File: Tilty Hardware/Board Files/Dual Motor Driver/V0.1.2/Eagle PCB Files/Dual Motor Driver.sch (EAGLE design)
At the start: 42 parts, among them J1 AVR_SPI_PRG_62X3_LOCK, Q1 16MHz, U1 ATMEGA328P, U2 L298_BRIDGE_DRIVER, U3 LM2931

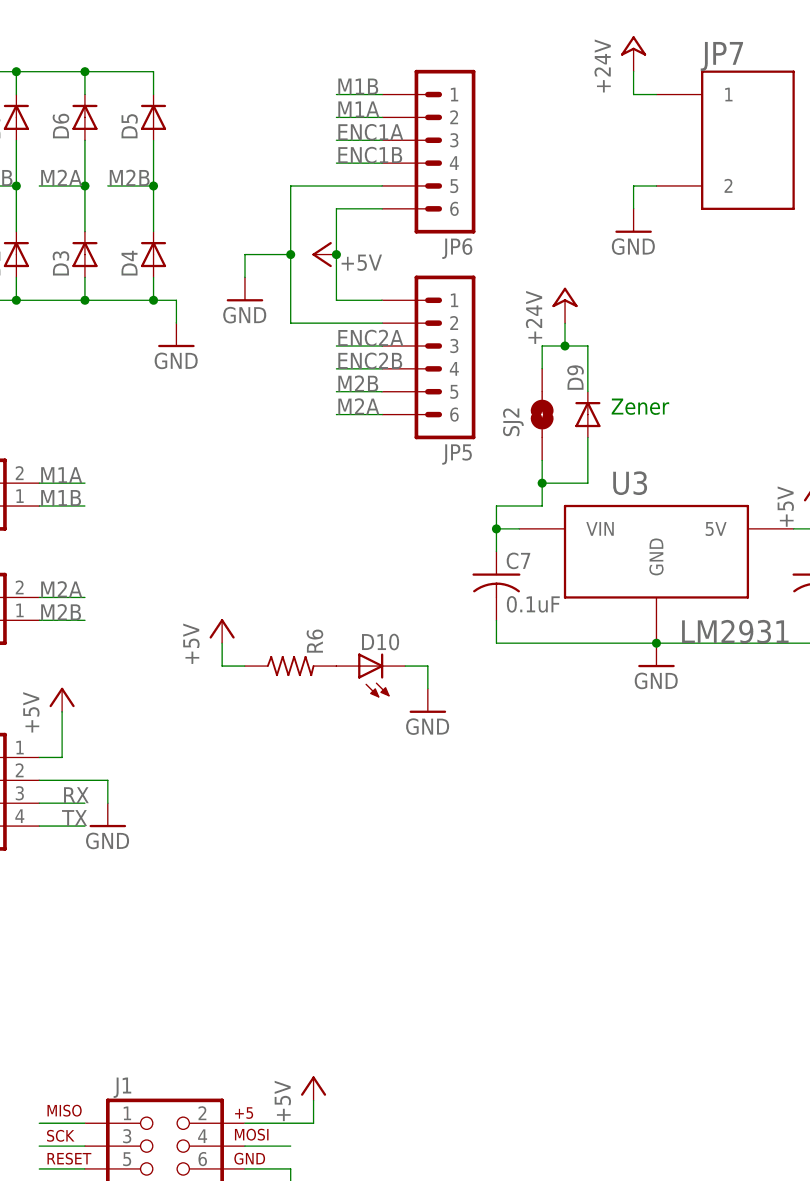
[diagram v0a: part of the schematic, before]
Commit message: Dula motor driver revisions
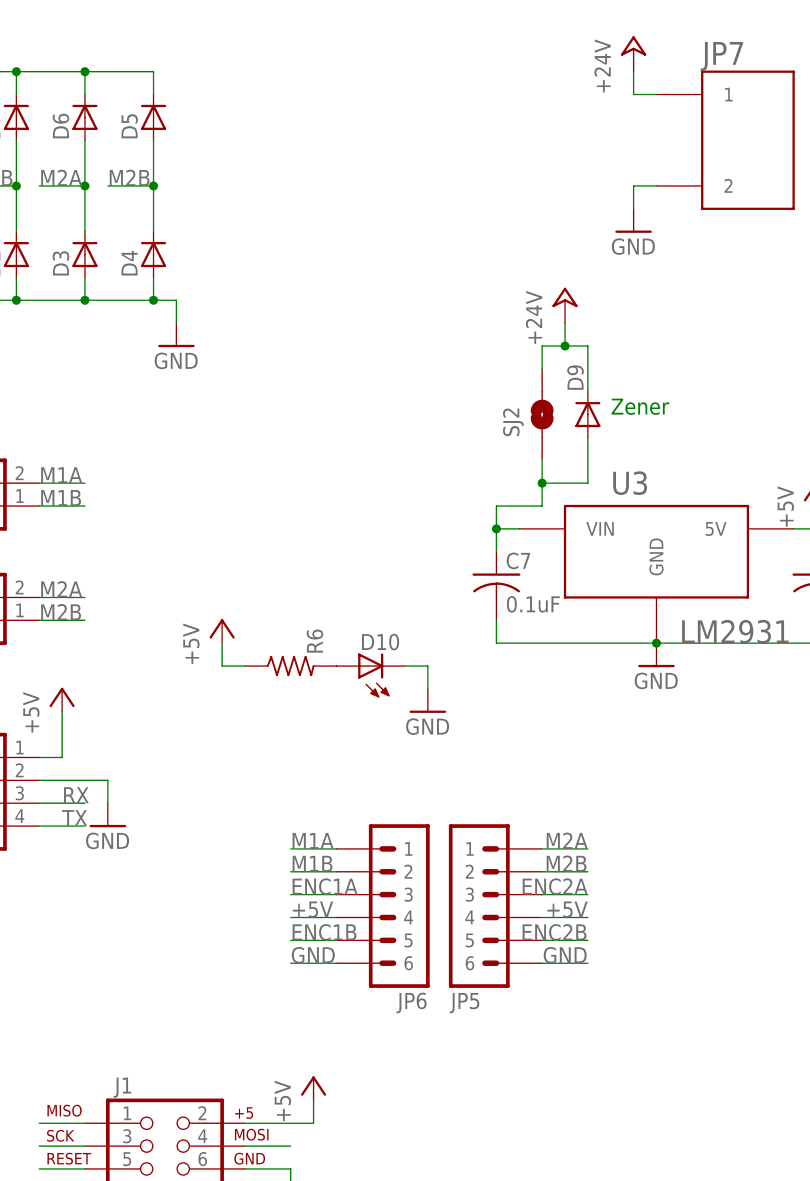
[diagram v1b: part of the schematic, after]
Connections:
- net +5V: now also JP5.4, JP6.4; no longer JP5.1, JP6.6
- net ENC1B: now also JP6.5; no longer JP6.4
- net ENC2B: now also JP5.5; no longer JP5.4
- net GND: now also JP5.6, JP6.6; no longer JP5.2, JP6.5
- net M1A: now also JP6.1; no longer JP6.2
- net M1B: now also JP6.2; no longer JP6.1
- net M2A: now also JP5.1; no longer JP5.6
- net M2B: now also JP5.2; no longer JP5.5
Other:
- moved on the sheet: JP5, JP6
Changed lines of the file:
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@@
 <part name="C8" library="resistor" deviceset="C-US" device="C0603" value="22pF"/>
 <part name="GND12" library="supply1" deviceset="GND" device=""/>
-<part name="P+11" library="supply1" deviceset="+5V" device=""/>
-<part name="GND7" library="supply1" deviceset="GND" device=""/>
 <part name="GND8" library="supply1" deviceset="GND" device=""/>
 <part name="S1" library="SparkFun-Electromechanical" deviceset="SWITCH-MOMENTARY-2" device="SMD"/>
@@
 <attribute name="PART#" x="137.16" y="119.38" size="1.778" layer="96" rot="R90" display="off"/>
 </instance>
-<instance part="JP5" gate="1" x="190.5" y="91.44" smashed="yes" rot="R180">
-<attribute name="PART#" x="190.5" y="91.44" size="1.778" layer="96" rot="R180" display="off"/>
-<attribute name="NAME" x="195.58" y="83.058" size="1.778" layer="95" rot="R180"/>
-</instance>
-<instance part="JP6" gate="1" x="190.5" y="114.3" smashed="yes" rot="R180">
-<attribute name="PART#" x="190.5" y="114.3" size="1.778" layer="96" rot="R180" display="off"/>
-<attribute name="NAME" x="195.58" y="105.918" size="1.778" layer="95" rot="R180"/>
+<instance part="JP5" gate="1" x="198.12" y="30.48" smashed="yes" rot="MR180">
+<attribute name="PART#" x="198.12" y="30.48" size="1.778" layer="96" rot="MR180" display="off"/>
+<attribute name="NAME" x="193.04" y="22.098" size="1.778" layer="95" rot="MR180"/>
+</instance>
+<instance part="JP6" gate="1" x="185.42" y="30.48" smashed="yes" rot="R180">
+<attribute name="PART#" x="185.42" y="30.48" size="1.778" layer="96" rot="R180" display="off"/>
+<attribute name="NAME" x="190.5" y="22.098" size="1.778" layer="95" rot="R180"/>
 </instance>
 <instance part="P+4" gate="1" x="129.54" y="127"/>
@@
 <instance part="C8" gate="G$1" x="35.56" y="43.18" rot="R90"/>
 <instance part="GND12" gate="1" x="25.4" y="35.56"/>
-<instance part="P+11" gate="1" x="177.8" y="104.14" smashed="yes" rot="R90">
-<attribute name="VALUE" x="185.42" y="104.14" size="1.778" layer="96" rot="R180"/>
-</instance>
-<instance part="GND7" gate="1" x="170.18" y="99.06"/>
 <instance part="GND8" gate="1" x="40.64" y="60.96"/>
 <instance part="S1" gate="G$1" x="45.72" y="66.04" smashed="yes">
@@
 </segment>
 <segment>
-<pinref part="GND7" gate="1" pin="GND"/>
-<wire x1="170.18" y1="101.6" x2="170.18" y2="104.14" width="0.1524" layer="91"/>
-<pinref part="JP6" gate="1" pin="5"/>
-<wire x1="175.26" y1="111.76" x2="185.42" y2="111.76" width="0.1524" layer="91"/>
-<pinref part="JP5" gate="1" pin="2"/>
-<wire x1="185.42" y1="96.52" x2="175.26" y2="96.52" width="0.1524" layer="91"/>
-<wire x1="175.26" y1="96.52" x2="175.26" y2="104.14" width="0.1524" layer="91"/>
-<wire x1="175.26" y1="104.14" x2="175.26" y2="111.76" width="0.1524" layer="91"/>
-<wire x1="170.18" y1="104.14" x2="175.26" y2="104.14" width="0.1524" layer="91"/>
-<junction x="175.26" y="104.14"/>
-</segment>
-<segment>
 <pinref part="U2" gate="G$1" pin="GND@20"/>
 <wire x1="99.06" y1="121.92" x2="99.06" y2="124.46" width="0.1524" layer="91"/>
@@
 <wire x1="134.62" y1="15.24" x2="137.16" y2="15.24" width="0.1524" layer="91"/>
 <wire x1="137.16" y1="15.24" x2="137.16" y2="12.7" width="0.1524" layer="91"/>
+</segment>
+<segment>
+<pinref part="JP6" gate="1" pin="6"/>
+<wire x1="180.34" y1="25.4" x2="175.26" y2="25.4" width="0.1524" layer="91"/>
+<label x="175.26" y="25.4" size="1.778" layer="95"/>
+</segment>
+<segment>
+<pinref part="JP5" gate="1" pin="6"/>
+<wire x1="203.2" y1="25.4" x2="208.28" y2="25.4" width="0.1524" layer="91"/>
+<label x="208.28" y="25.4" size="1.778" layer="95" rot="MR0"/>
 </segment>
 </net>
@@
 </segment>
 <segment>
-<pinref part="JP6" gate="1" pin="2"/>
-<wire x1="185.42" y1="119.38" x2="180.34" y2="119.38" width="0.1524" layer="91"/>
-<label x="180.34" y="119.38" size="1.778" layer="95"/>
-</segment>
-<segment>
 <pinref part="JP9" gate="G$1" pin="2"/>
 <wire x1="147.32" y1="78.74" x2="152.4" y2="78.74" width="0.1524" layer="91"/>
 <label x="147.32" y="78.74" size="1.778" layer="95"/>
+</segment>
+<segment>
+<pinref part="JP6" gate="1" pin="1"/>
+<wire x1="180.34" y1="38.1" x2="175.26" y2="38.1" width="0.1524" layer="91"/>
+<label x="175.26" y="38.1" size="1.778" layer="95"/>
 </segment>
 </net>
@@
 </segment>
 <segment>
-<pinref part="JP6" gate="1" pin="1"/>
-<wire x1="185.42" y1="121.92" x2="180.34" y2="121.92" width="0.1524" layer="91"/>
-<label x="180.34" y="121.92" size="1.778" layer="95"/>
-</segment>
-<segment>
 <pinref part="JP9" gate="G$1" pin="1"/>
 <wire x1="147.32" y1="76.2" x2="152.4" y2="76.2" width="0.1524" layer="91"/>
 <label x="147.32" y="76.2" size="1.778" layer="95"/>
+</segment>
+<segment>
+<pinref part="JP6" gate="1" pin="2"/>
+<wire x1="180.34" y1="35.56" x2="175.26" y2="35.56" width="0.1524" layer="91"/>
+<label x="175.26" y="35.56" size="1.778" layer="95"/>
 </segment>
 </net>
@@
 </segment>
 <segment>
-<pinref part="JP5" gate="1" pin="6"/>
-<wire x1="185.42" y1="86.36" x2="180.34" y2="86.36" width="0.1524" layer="91"/>
-<label x="180.34" y="86.36" size="1.778" layer="95"/>
-</segment>
-<segment>
 <pinref part="JP10" gate="G$1" pin="2"/>
 <wire x1="147.32" y1="66.04" x2="152.4" y2="66.04" width="0.1524" layer="91"/>
 <label x="147.32" y="66.04" size="1.778" layer="95"/>
+</segment>
+<segment>
+<pinref part="JP5" gate="1" pin="1"/>
+<wire x1="203.2" y1="38.1" x2="208.28" y2="38.1" width="0.1524" layer="91"/>
+<label x="208.28" y="38.1" size="1.778" layer="95" rot="MR0"/>
 </segment>
 </net>
@@
 </segment>
 <segment>
-<pinref part="JP5" gate="1" pin="5"/>
-<wire x1="185.42" y1="88.9" x2="180.34" y2="88.9" width="0.1524" layer="91"/>
-<label x="180.34" y="88.9" size="1.778" layer="95"/>
-</segment>
-<segment>
 <pinref part="JP10" gate="G$1" pin="1"/>
 <wire x1="147.32" y1="63.5" x2="152.4" y2="63.5" width="0.1524" layer="91"/>
 <label x="147.32" y="63.5" size="1.778" layer="95"/>
+</segment>
+<segment>
+<pinref part="JP5" gate="1" pin="2"/>
+<wire x1="203.2" y1="35.56" x2="208.28" y2="35.56" width="0.1524" layer="91"/>
+<label x="208.28" y="35.56" size="1.778" layer="95" rot="MR0"/>
 </segment>
 </net>
@@
 </segment>
 <segment>
-<pinref part="JP5" gate="1" pin="1"/>
-<wire x1="185.42" y1="99.06" x2="180.34" y2="99.06" width="0.1524" layer="91"/>
-<pinref part="P+11" gate="1" pin="+5V"/>
-<wire x1="180.34" y1="99.06" x2="180.34" y2="104.14" width="0.1524" layer="91"/>
-<pinref part="JP6" gate="1" pin="6"/>
-<wire x1="185.42" y1="109.22" x2="180.34" y2="109.22" width="0.1524" layer="91"/>
-<wire x1="180.34" y1="104.14" x2="180.34" y2="109.22" width="0.1524" layer="91"/>
-<junction x="180.34" y="104.14"/>
-</segment>
-<segment>
 <pinref part="P+3" gate="1" pin="+5V"/>
 <pinref part="U1" gate="G$1" pin="AVCC"/>
@@
 <junction x="121.92" y="66.04"/>
 </segment>
+<segment>
+<pinref part="JP6" gate="1" pin="4"/>
+<wire x1="180.34" y1="30.48" x2="175.26" y2="30.48" width="0.1524" layer="91"/>
+<label x="175.26" y="30.48" size="1.778" layer="95"/>
+</segment>
+<segment>
+<pinref part="JP5" gate="1" pin="4"/>
+<wire x1="203.2" y1="30.48" x2="208.28" y2="30.48" width="0.1524" layer="91"/>
+<label x="208.28" y="30.48" size="1.778" layer="95" rot="MR0"/>
+</segment>
 </net>
 <net name="RESET" class="0">
@@
 <net name="ENC1B" class="0">
 <segment>
-<pinref part="JP6" gate="1" pin="4"/>
-<wire x1="185.42" y1="114.3" x2="180.34" y2="114.3" width="0.1524" layer="91"/>
-<label x="180.34" y="114.3" size="1.778" layer="95"/>
-</segment>
-<segment>
 <pinref part="U1" gate="G$1" pin="PC1(ADC1)"/>
 <wire x1="101.6" y1="63.5" x2="111.76" y2="63.5" width="0.1524" layer="91"/>
 <label x="104.14" y="63.5" size="1.778" layer="95"/>
 </segment>
+<segment>
+<pinref part="JP6" gate="1" pin="5"/>
+<wire x1="180.34" y1="27.94" x2="175.26" y2="27.94" width="0.1524" layer="91"/>
+<label x="175.26" y="27.94" size="1.778" layer="95"/>
+</segment>
 </net>
 <net name="ENC1A" class="0">
 <segment>
 <pinref part="JP6" gate="1" pin="3"/>
-<wire x1="185.42" y1="116.84" x2="180.34" y2="116.84" width="0.1524" layer="91"/>
-<label x="180.34" y="116.84" size="1.778" layer="95"/>
+<wire x1="180.34" y1="33.02" x2="175.26" y2="33.02" width="0.1524" layer="91"/>
+<label x="175.26" y="33.02" size="1.778" layer="95"/>
 </segment>
 <segment>
@@
 <net name="ENC2B" class="0">
 <segment>
-<pinref part="JP5" gate="1" pin="4"/>
-<wire x1="185.42" y1="91.44" x2="180.34" y2="91.44" width="0.1524" layer="91"/>
-<label x="180.34" y="91.44" size="1.778" layer="95"/>
-</segment>
-<segment>
 <pinref part="U1" gate="G$1" pin="PD3(INT1)"/>
 <wire x1="101.6" y1="35.56" x2="111.76" y2="35.56" width="0.1524" layer="91"/>
 <label x="104.14" y="35.56" size="1.778" layer="95"/>
 </segment>
+<segment>
+<pinref part="JP5" gate="1" pin="5"/>
+<wire x1="203.2" y1="27.94" x2="208.28" y2="27.94" width="0.1524" layer="91"/>
+<label x="208.28" y="27.94" size="1.778" layer="95" rot="MR0"/>
+</segment>
 </net>
 <net name="ENC2A" class="0">
-<segment>
-<pinref part="JP5" gate="1" pin="3"/>
-<wire x1="185.42" y1="93.98" x2="180.34" y2="93.98" width="0.1524" layer="91"/>
-<label x="180.34" y="93.98" size="1.778" layer="95"/>
-</segment>
 <segment>
 <pinref part="U1" gate="G$1" pin="PC0(ADC0)"/>
@@
 <label x="104.14" y="66.04" size="1.778" layer="95"/>
 </segment>
-</net>
+<segment>
+<pinref part="JP5" gate="1" pin="3"/>
+<wire x1="203.2" y1="33.02" x2="208.28" y2="33.02" width="0.1524" layer="91"/>
+<label x="208.28" y="33.02" size="1.778" layer="95" rot="MR0"/>
+</segment>
+</net>
